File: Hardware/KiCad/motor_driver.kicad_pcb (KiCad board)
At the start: 2 copper layers, 69.6 x 75.7 mm, 17 parts, among them J1 Conn_01x02, J10 m4, J11 m5, J12 m6, J13 Conn_01x03, J14 power12v, J2 Conn_01x02, J3 Conn_01x02, J4 Conn_01x02, J5 Conn_01x02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

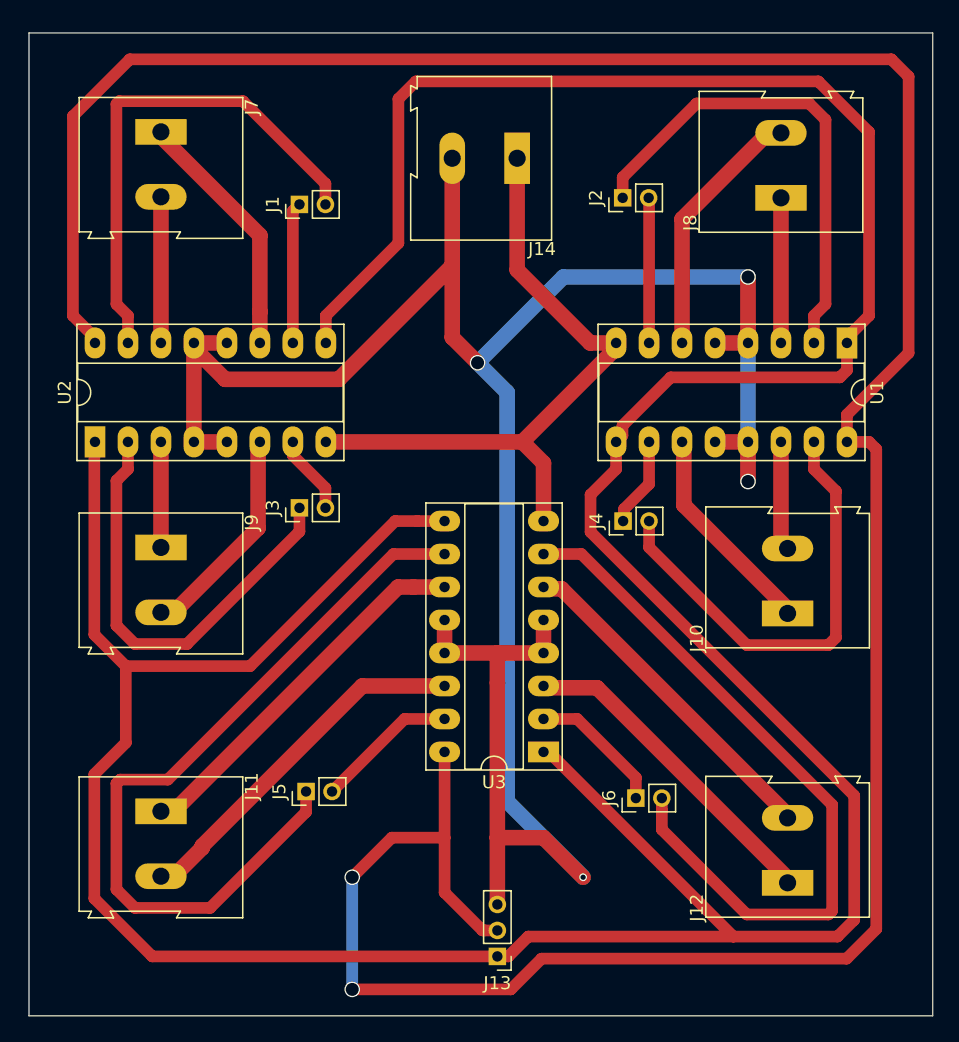
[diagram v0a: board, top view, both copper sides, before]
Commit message: Modified PCB and added link to txt
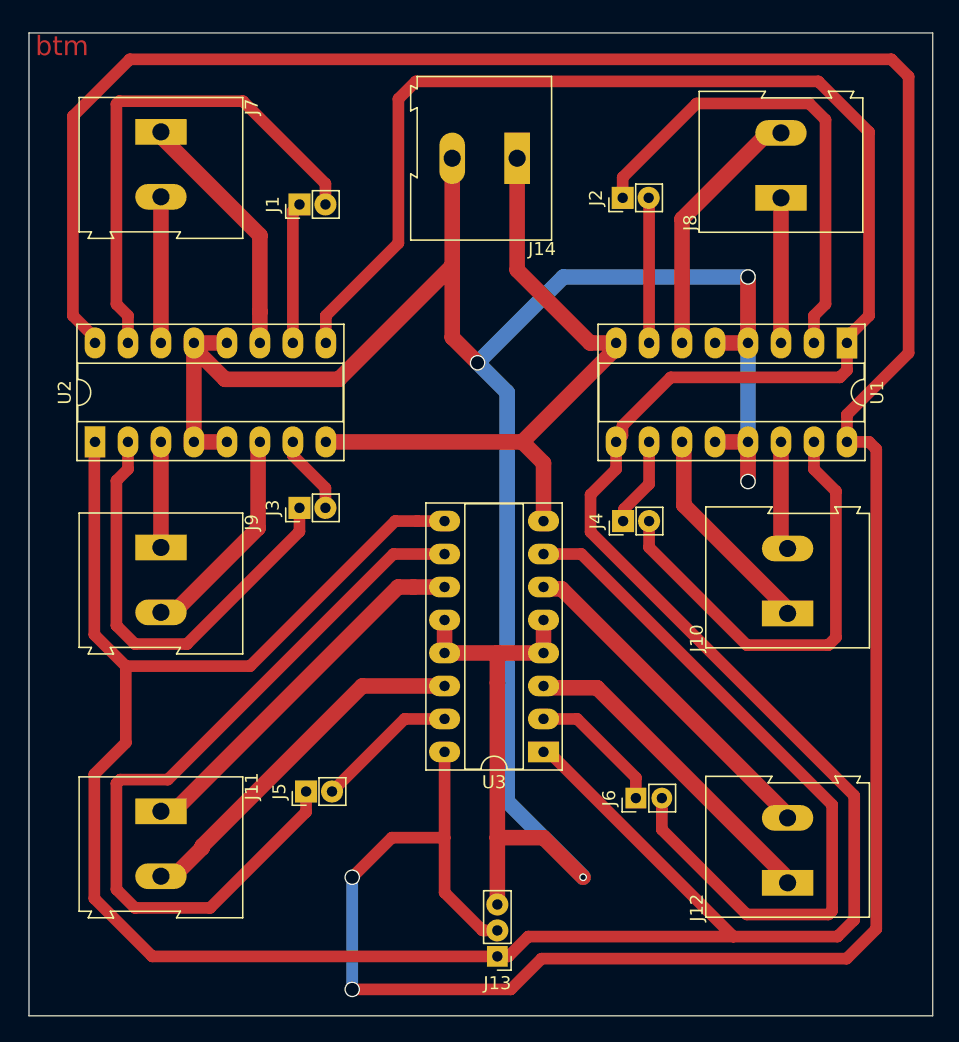
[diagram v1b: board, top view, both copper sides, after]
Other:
- board text added: "btm"
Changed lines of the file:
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@@
-(kicad_pcb (version 4) (host pcbnew 4.0.7-e2-6376~58~ubuntu16.04.1)
+(kicad_pcb (version 4) (host pcbnew 4.0.2+dfsg1-stable)
   (general
     (links 49)
-    (no_connects 49)
-    (area 50.114999 50.749999 125.145001 126.415001)
+    (no_connects 0)
+    (area 53.289999 50.316 122.986001 126.542001)
     (thickness 1.6)
-    (drawings 4)
+    (drawings 5)
     (tracks 205)
     (zones 0)
@@
     (mod_text_size 1 1)
     (mod_text_width 0.15)
-    (pad_size 1.5 1.5)
-    (pad_drill 0.6)
+    (pad_size 1.7 1.7)
+    (pad_drill 0.8)
     (pad_to_mask_clearance 0)
     (aux_axis_origin 0 0)
@@
       (effects (font (size 1 1) (thickness 0.15)))
     )
-    (pad 1 thru_hole rect (at 0 0 90) (size 1.35 1.35) (drill 0.8) (layers *.Cu *.Mask)
+    (pad 1 thru_hole rect (at 0 0 90) (size 1.7 1.7) (drill 0.8) (layers *.Cu *.Mask)
       (net 1 pwm_m1))
-    (pad 2 thru_hole oval (at 0 2 90) (size 1.35 1.35) (drill 0.8) (layers *.Cu *.Mask)
+    (pad 2 thru_hole oval (at 0 2 90) (size 1.7 1.7) (drill 0.8) (layers *.Cu *.Mask)
       (net 2 dig_m1))
     (model ${KISYS3DMOD}/Pin_Headers.3dshapes/Pin_Header_Straight_1x02_Pitch2.00mm.wrl
@@
       (effects (font (size 1 1) (thickness 0.15)))
     )
-    (pad 1 thru_hole rect (at 0 0 90) (size 1.35 1.35) (drill 0.8) (layers *.Cu *.Mask)
+    (pad 1 thru_hole rect (at 0 0 90) (size 1.7 1.7) (drill 0.8) (layers *.Cu *.Mask)
       (net 3 pwm_m2))
-    (pad 2 thru_hole oval (at 0 2 90) (size 1.35 1.35) (drill 0.8) (layers *.Cu *.Mask)
+    (pad 2 thru_hole oval (at 0 2 90) (size 1.7 1.7) (drill 0.8) (layers *.Cu *.Mask)
       (net 4 dig_m2))
     (model ${KISYS3DMOD}/Pin_Headers.3dshapes/Pin_Header_Straight_1x02_Pitch2.00mm.wrl
@@
       (effects (font (size 1 1) (thickness 0.15)))
     )
-    (pad 1 thru_hole rect (at 0 0 90) (size 1.35 1.35) (drill 0.8) (layers *.Cu *.Mask)
+    (pad 1 thru_hole rect (at 0 0 90) (size 1.7 1.7) (drill 0.8) (layers *.Cu *.Mask)
       (net 5 pwm_m3))
-    (pad 2 thru_hole oval (at 0 2 90) (size 1.35 1.35) (drill 0.8) (layers *.Cu *.Mask)
+    (pad 2 thru_hole oval (at 0 2 90) (size 1.7 1.7) (drill 0.8) (layers *.Cu *.Mask)
       (net 6 dig_m3))
     (model ${KISYS3DMOD}/Pin_Headers.3dshapes/Pin_Header_Straight_1x02_Pitch2.00mm.wrl
@@
       (effects (font (size 1 1) (thickness 0.15)))
     )
-    (pad 1 thru_hole rect (at 0 0 90) (size 1.35 1.35) (drill 0.8) (layers *.Cu *.Mask)
+    (pad 1 thru_hole rect (at 0 0 90) (size 1.7 1.7) (drill 0.8) (layers *.Cu *.Mask)
       (net 7 pwm_m4))
-    (pad 2 thru_hole oval (at 0 2 90) (size 1.35 1.35) (drill 0.8) (layers *.Cu *.Mask)
+    (pad 2 thru_hole oval (at 0 2 90) (size 1.7 1.7) (drill 0.8) (layers *.Cu *.Mask)
       (net 8 dig_m4))
     (model ${KISYS3DMOD}/Pin_Headers.3dshapes/Pin_Header_Straight_1x02_Pitch2.00mm.wrl
@@
       (effects (font (size 1 1) (thickness 0.15)))
     )
-    (pad 1 thru_hole rect (at 0 0 90) (size 1.35 1.35) (drill 0.8) (layers *.Cu *.Mask)
+    (pad 1 thru_hole rect (at 0 0 90) (size 1.7 1.7) (drill 0.8) (layers *.Cu *.Mask)
       (net 9 pwm_m5))
-    (pad 2 thru_hole oval (at 0 2 90) (size 1.35 1.35) (drill 0.8) (layers *.Cu *.Mask)
+    (pad 2 thru_hole oval (at 0 2 90) (size 1.7 1.7) (drill 0.8) (layers *.Cu *.Mask)
       (net 10 dig_m5))
     (model ${KISYS3DMOD}/Pin_Headers.3dshapes/Pin_Header_Straight_1x02_Pitch2.00mm.wrl
@@
       (effects (font (size 1 1) (thickness 0.15)))
     )
-    (pad 1 thru_hole rect (at 0 0 90) (size 1.35 1.35) (drill 0.8) (layers *.Cu *.Mask)
+    (pad 1 thru_hole rect (at 0 0 90) (size 1.6 1.6) (drill 0.8) (layers *.Cu *.Mask)
       (net 11 pwm_m6))
-    (pad 2 thru_hole oval (at 0 2 90) (size 1.35 1.35) (drill 0.8) (layers *.Cu *.Mask)
+    (pad 2 thru_hole oval (at 0 2 90) (size 1.6 1.6) (drill 0.8) (layers *.Cu *.Mask)
       (net 12 dig_m6))
     (model ${KISYS3DMOD}/Pin_Headers.3dshapes/Pin_Header_Straight_1x02_Pitch2.00mm.wrl
@@
       (effects (font (size 1 1) (thickness 0.15)))
     )
-    (pad 1 thru_hole rect (at 0 0 180) (size 1.35 1.35) (drill 0.8) (layers *.Cu *.Mask)
+    (pad 1 thru_hole rect (at 0 0 180) (size 1.6 1.6) (drill 0.8) (layers *.Cu *.Mask)
       (net 25 en))
-    (pad 2 thru_hole oval (at 0 2 180) (size 1.35 1.35) (drill 0.8) (layers *.Cu *.Mask)
+    (pad 2 thru_hole oval (at 0 2 180) (size 1.7 1.7) (drill 0.8) (layers *.Cu *.Mask)
       (net 26 ardu5V))
-    (pad 3 thru_hole oval (at 0 4 180) (size 1.35 1.35) (drill 0.8) (layers *.Cu *.Mask)
+    (pad 3 thru_hole oval (at 0 4 180) (size 1.7 1.7) (drill 0.8) (layers *.Cu *.Mask)
       (net 27 GND))
     (model ${KISYS3DMOD}/Pin_Headers.3dshapes/Pin_Header_Straight_1x03_Pitch2.00mm.wrl
@@
     )
   )
+  (gr_text btm (at 55.88 51.816) (layer F.Cu)
+    (effects (font (size 1.5 1.5) (thickness 0.3)))
+  )
   (gr_line (start 122.936 50.8) (end 53.34 50.8) (layer Edge.Cuts) (width 0.1))

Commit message: motor driver pcb mkII
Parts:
- added J15: Conn_01x01, Pin_Headers:Pin_Header_Straight_1x01_Pitch2.00mm, F.Cu at (89.4, 121.4)
- added J16: Conn_01x01, Pin_Headers:Pin_Header_Straight_1x01_Pitch2.00mm, F.Cu at (108.7, 71.1)
- added J16: Conn_01x01, Pin_Headers:Pin_Header_Straight_1x01_Pitch2.00mm, F.Cu at (108.7, 85.3)
- added J16: Conn_01x01, Pin_Headers:Pin_Header_Straight_1x01_Pitch2.00mm, F.Cu at (85.9, 74.7)
- moved J5 7.75 mm to (77.8, 116.3)
- moved J6 7.27 mm to (98.6, 116.8)
- moved J13 5.59 mm to (89.4, 116.3)
- moved J4 2.00 mm to (101.1, 88.4)
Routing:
- net GND: track 189.3 -> 0.40 mm, vias 4 -> 0
- net ardu5V: track 229.8 -> 202.8 mm, vias 2 -> 0
- net en: track 293.5 -> 303.7 mm
- net pwm_m2: track 37.6 -> 44.4 mm
- net pwm_m6: track 10.6 -> 16.8 mm
- net pwm_m3: track 34.6 -> 40.6 mm
- net dig_m1: track 39.2 -> 45.0 mm
- net pwm_m5: track 60.6 -> 66.0 mm
- net dig_m5: track 11.0 -> 16.3 mm
- net m6-: track 26.3 -> 30.7 mm
- net dig_m4: track 35.5 -> 39.9 mm
- net dig_m6: track 56.7 -> 60.1 mm
- net m6+: track 25.3 -> 28.6 mm
- net m1+: track 19.4 -> 22.7 mm
- net m4+: track 16.6 -> 19.2 mm
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- added copper zone on F.Cu, net GND
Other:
- board text removed: "btm"

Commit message: added text
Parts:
- removed J15, J16 (x3): Conn_01x01, Pin_Headers:Pin_Header_Straight_1x01_Pitch2.00mm
- moved J5 4.70 mm to (74.7, 119.9)
- moved J6 2.03 mm to (98.6, 114.8)
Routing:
- net ardu5V: track 202.8 -> 127.9 mm
- net dig_m5: track 16.3 -> 21.2 mm
- net pwm_m5: track 66.0 -> 61.4 mm
- net pwm_m6: track 16.8 -> 14.8 mm
- net dig_m6: track 60.1 -> 62.1 mm
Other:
- board text added: "motor driver"
